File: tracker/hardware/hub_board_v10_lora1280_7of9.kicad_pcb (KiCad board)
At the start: 4 copper layers, 72 x 80 mm, 49 parts, among them U1 U1, U2 U2, U3 U3, U5 U5, U6 U6, U7 U7

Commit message: fix(hub): the operator's routing was 37 copper GRAPHICS, not tracks -- convert and locate the 5 violations
MEASURED, and it explains two separate symptoms the operator reported:

  "the mouse currently doesn't select them successfully"

His interactive pass produced NO track segments. It produced 37 `gr_line` graphics on copper layers,
each carrying a net: /SPI1_SCK 18, /E28_DIO3 7, /E28_BUSY 4, /E28_RESET_N 3, /I2C_SCL 2, /E28_DIO1 2,
/I2C_SDA 1. KiCad treats a net-aware graphic as conductive, so connectivity and DRC both looked
satisfied and no unconnected item named SPI1_SCK or E28_DIO3 -- the nets really are connected.

But a graphic is not a track:
  * selection is governed by the GRAPHICS filter, not TRACKS, which is exactly why clicking one with
    only Tracks enabled selects nothing (and why a finer grid was never going to help);
  * pressing D/M treats it as a drawing, not a routed track, so it does not behave as hand-routing;
  * the interactive router will not shove or re-route it;
  * every tool here that walks board.GetTracks() -- both maze routers, the rip-up pass, the grid and
    validator tests, the connectivity census -- CANNOT SEE THE NET AT ALL. "9/9 routed" was true for
    KiCad and false for our automation, which is the worse kind of green.

FIX: tracker/hardware/tmp_probes/graphics_to_tracks.py recreates each graphic as a PCB_TRACK with the
same layer, width and endpoints (arcs segmented), then deletes the graphic. Applied: 37 graphics ->
37 tracks, and DRC is bit-for-bit unchanged afterwards -- 79 violations, 5 clearance, 0 shorts,
0 mask bridges, same 86 unconnected. So the conversion cost nothing and every net is now visible to
the tooling.

THE FIVE VIOLATIONS, LOCATED PROPERLY
The DRC report's item `pos` is the object's own reference point, NOT the closest approach. The first
figure I drew put its markers ~3 mm off the real gaps; a vision review rejected it while the numbers
were right. tracker/hardware/tmp_probes/plot_clearance_violati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
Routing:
- net /SPI1_SCK: track 0.00 -> 50.7 mm
- net /E28_DIO3: track 0.00 -> 37.9 mm
- net /I2C_SCL: track 27.2 -> 44.9 mm
- net /E28_RESET_N: track 54.4 -> 70.7 mm
- net /E28_DIO1: track 57.4 -> 73.3 mm
- net /E28_BUSY: track 42.7 -> 53.8 mm
- net /I2C_SDA: track 45.4 -> 48.5 mm

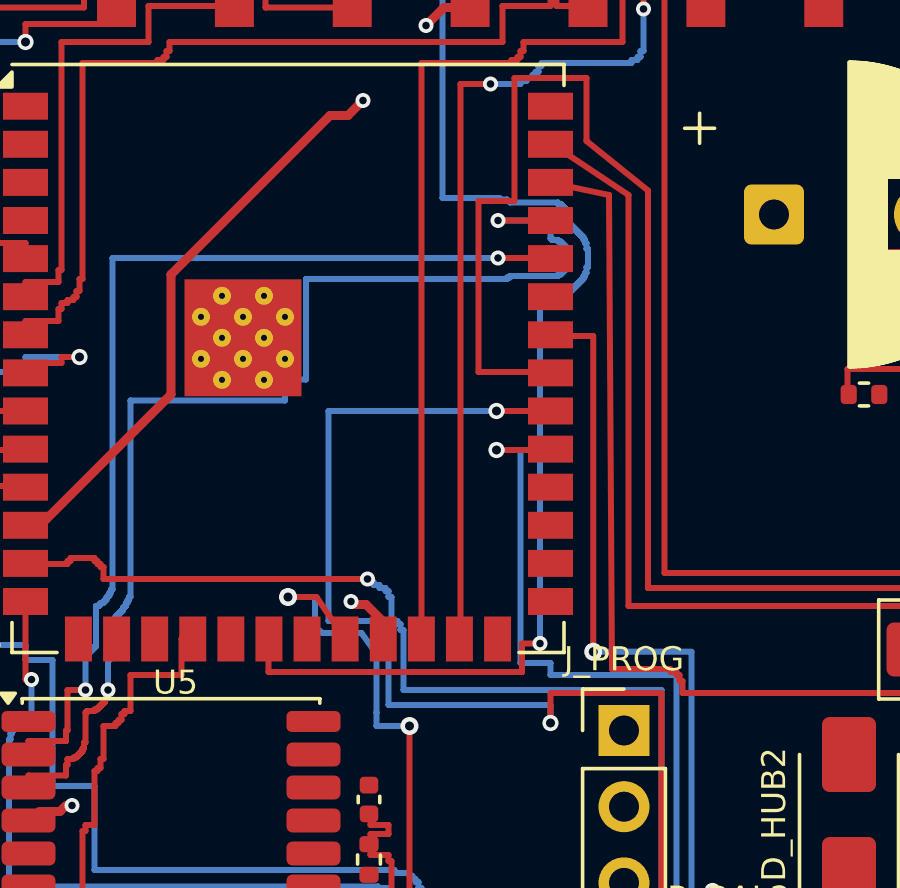
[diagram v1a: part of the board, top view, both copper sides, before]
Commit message: fix(hub): clear the 5 clearance violations on the LoRa1280 interface
Nudged the three corridors: I2C_SDA/I2C_SCL (0.1606 -> >=0.200),
SPI1_SCK/E28_RESET_N on B.Cu (0.1487), and SPI1_SCK vs U1 pad 21
F33_VSENSE (0.1533). Zones refilled before DRC. No rule relaxation.
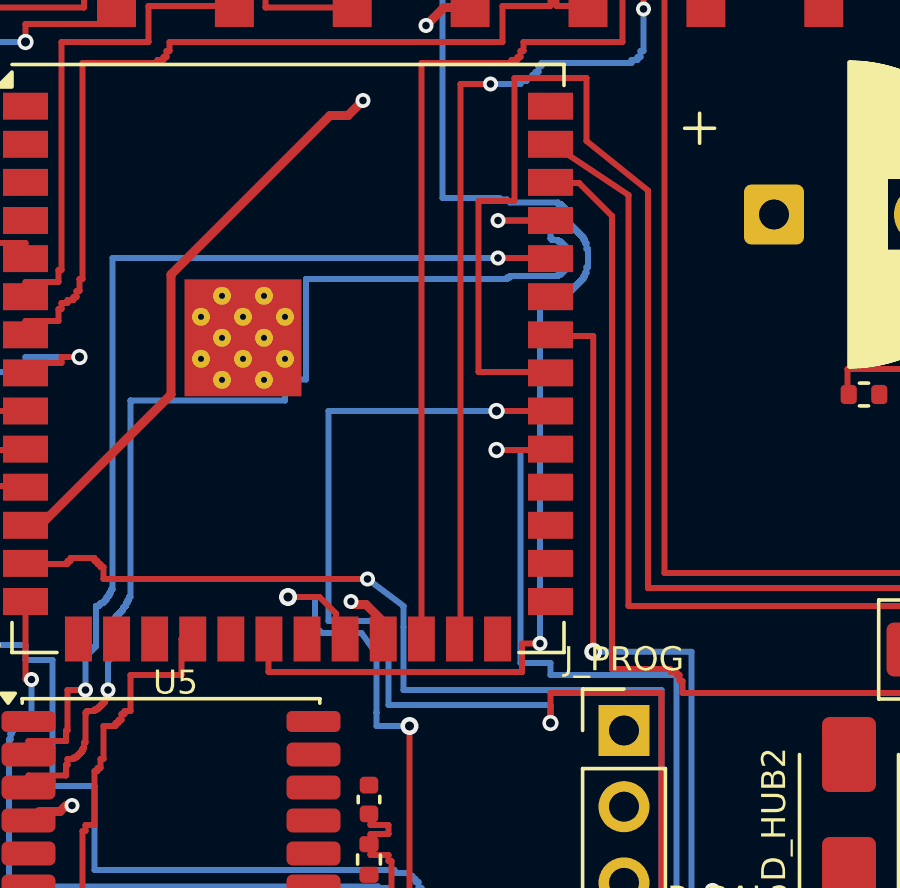
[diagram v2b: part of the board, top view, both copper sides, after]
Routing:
- net /USB_DN: track 36.1 -> 33.4 mm
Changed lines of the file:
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@@
 		)
 	)
+	(gr_line
+		(start 23.65 50.55)
+		(end 22.45 49.65)
+		(stroke
+			(width 0.2)
+			(type default)
+		)
+		(layer "B.Cu")
+		(net 47)
+	)
+	(gr_line
+		(start 23.65 51.25)
+		(end 23.65 50.55)
+		(stroke
+			(width 0.2)
+			(type default)
+		)
+		(layer "B.Cu")
+		(net 47)
+	)
 	(gr_rect
 		(start 0 0)
@@
 	)
 	(segment
-		(start 32.55 52.65)
-		(end 32.55 52.75)
+		(start 54.25 54.95)
+		(end 55.45 54.95)
 		(width 0.2)
 		(layer "F.Cu")
@@
 	)
 	(segment
-		(start 54.25 54.15)
-		(end 54.25 54.95)
+		(start 51.05 53.45)
+		(end 51.05 54.15)
 		(width 0.2)
 		(layer "F.Cu")
@@
 	)
 	(segment
-		(start 51.05 54.15)
-		(end 54.25 54.15)
+		(start 29.5 36.45)
+		(end 30.6 37.55)
 		(width 0.2)
 		(layer "F.Cu")
@@
 	)
 	(segment
-		(start 32.75 52.85)
-		(end 32.85 52.85)
+		(start 32.85 53.05)
+		(end 32.95 53.05)
 		(width 0.2)
 		(layer "F.Cu")
@@
 	)
 	(segment
-		(start 32.75 52.75)
-		(end 32.75 52.85)
+		(start 32.95 53.05)
+		(end 32.95 53.45)
 		(width 0.2)
 		(layer "F.Cu")
@@
 	)
 	(segment
-		(start 32.95 53.05)
-		(end 32.95 53.45)
+		(start 32.55 52.65)
+		(end 32.55 52.75)
 		(width 0.2)
 		(layer "F.Cu")
@@
 	)
 	(segment
-		(start 28.6 36.45)
-		(end 30.5 36.85)
+		(start 30.6 37.55)
+		(end 30.6 52.65)
 		(width 0.2)
 		(layer "F.Cu")
@@
 	)
 	(segment
-		(start 54.25 54.95)
-		(end 55.45 54.95)
+		(start 32.95 53.45)
+		(end 51.05 53.45)
 		(width 0.2)
 		(layer "F.Cu")
@@
 	)
 	(segment
-		(start 32.95 53.45)
-		(end 51.05 53.45)
+		(start 32.75 52.85)
+		(end 32.85 52.85)
 		(width 0.2)
 		(layer "F.Cu")
@@
 	)
 	(segment
-		(start 51.05 53.45)
-		(end 51.05 54.15)
+		(start 32.85 52.85)
+		(end 32.85 53.05)
 		(width 0.2)
 		(layer "F.Cu")
@@
 	)
 	(segment
-		(start 32.85 53.05)
-		(end 32.95 53.05)
+		(start 32.55 52.75)
+		(end 32.75 52.75)
 		(width 0.2)
 		(layer "F.Cu")
@@
 	)
 	(segment
-		(start 30.5 36.85)
-		(end 30.6 52.65)
+		(start 28.6 36.45)
+		(end 29.5 36.45)
 		(width 0.2)
 		(layer "F.Cu")
@@
 	)
 	(segment
-		(start 30.6 52.65)
-		(end 32.55 52.65)
+		(start 54.25 54.15)
+		(end 54.25 54.95)
 		(width 0.2)
 		(layer "F.Cu")
@@
 	)
 	(segment
-		(start 32.85 52.85)
-		(end 32.85 53.05)
+		(start 32.75 52.75)
+		(end 32.75 52.85)
 		(width 0.2)
 		(layer "F.Cu")
@@
 	)
 	(segment
-		(start 32.55 52.75)
-		(end 32.75 52.75)
+		(start 30.6 52.65)
+		(end 32.55 52.65)
+		(width 0.2)
+		(layer "F.Cu")
+		(net 22)
+	)
+	(segment
+		(start 51.05 54.15)
+		(end 54.25 54.15)
 		(width 0.2)
 		(layer "F.Cu")
@@
 	)
 	(segment
-		(start 22.75 51.05)
-		(end 21.15 51.05)
-		(width 0.2)
-		(layer "B.Cu")
-		(net 33)
-	)
-	(segment
 		(start 48.55 64.45)
 		(end 48.55 62.45)
@@
 	)
 	(segment
-		(start 23.15 53.85)
-		(end 23.15 51.85)
-		(width 0.2)
-		(layer "B.Cu")
-		(net 33)
-	)
-	(segment
-		(start 28.55 53.85)
-		(end 23.15 53.85)
+		(start 22.55 51.05)
+		(end 21.15 51.05)
 		(width 0.2)
 		(layer "B.Cu")
@@
 	)
 	(segment
-		(start 23.05 51.85)
-		(end 23.05 51.65)
+		(start 23.15 53.85)
+		(end 23.15 51.65)
 		(width 0.2)
 		(layer "B.Cu")
@@
 	)
 	(segment
-		(start 22.95 51.65)
-		(end 22.95 51.55)
-		(width 0.2)
-		(layer "B.Cu")
-		(net 33)
-	)
-	(segment
 		(start 21.15 44.05)
 		(end 26.75 44.05)
@@
 	)
 	(segment
-		(start 23.05 51.65)
-		(end 22.95 51.65)
+		(start 35.175 62.45)
+		(end 48.55 62.45)
 		(width 0.2)
 		(layer "B.Cu")
@@
 	)
 	(segment
-		(start 22.75 51.55)
-		(end 22.75 51.05)
+		(start 23.15 51.65)
+		(end 22.55 51.05)
 		(width 0.2)
 		(layer "B.Cu")
@@
 	)
 	(segment
-		(start 22.95 51.55)
-		(end 22.75 51.55)
-		(width 0.2)
-		(layer "B.Cu")
-		(net 33)
-	)
-	(segment
-		(start 35.175 62.45)
-		(end 48.55 62.45)
+		(start 28.55 53.85)
+		(end 23.15 53.85)
 		(width 0.2)
 		(layer "B.Cu")
@@
 	)
 	(segment
-		(start 23.15 51.85)
-		(end 23.05 51.85)
+		(start 21.7 51.65)
+		(end 21.4 51.35)
 		(width 0.2)
-		(layer "B.Cu")
-		(net 33)
+		(layer "F.Cu")
+		(net 34)
 	)
 	(segment
-		(start 43.8 73)
-		(end 45.7 73)
+		(start 21.4 51.35)
+		(end 21.4 50.8)
 		(width 0.2)
 		(layer "F.Cu")
@@
 	)
 	(segment
-		(start 20.75 50.25)
-		(end 19.8 50.25)
+		(start 43.8 73)
+		(end 45.7 73)
 		(width 0.2)
 		(layer "F.Cu")
@@
 	)
 	(segment
-		(start 29.15 61.85)
-		(end 29.15 69.15)
+		(start 21.4 50.8)
+		(end 20.85 50.25)
 		(width 0.2)
 		(layer "F.Cu")
@@
 	)
 	(segment
-		(start 21.7 51.65)
-		(end 20.75 50.25)
+		(start 20.85 50.25)
+		(end 19.8 50.25)
+		(width 0.2)
+		(layer "F.Cu")
+		(net 34)
+	)
+	(segment
+		(start 29.15 61.85)
+		(end 29.15 69.15)
 		(width 0.2)
 		(layer "F.Cu")
@@
 	)
 	(segment
-		(start 23.45 51.05)
-		(end 23.45 51.15)
-		(width 0.2)
-		(layer "B.Cu")
-		(net 47)
-	)
-	(segment
-		(start 23.15 50.05)
-		(end 23.15 50.25)
-		(width 0.2)
-		(layer "B.Cu")
-		(net 47)
-	)
-	(segment
-		(start 22.45 49.75)
-		(end 22.65 49.75)
+		(start 30.95 61.05)
+		(end 30.95 62.35)
 		(width 0.2)
 		(layer "B.Cu")
@@
 	)
 	(segment
-		(start 23.65 53.35)
-		(end 32.25 53.35)
+		(start 32.25 61.05)
+		(end 30.95 61.05)
 		(width 0.2)
 		(layer "B.Cu")
@@
 	)
 	(segment
-		(start 22.65 49.85)
-		(end 22.85 49.85)
+		(start 23.65 51.25)
+		(end 23.65 53.35)
 		(width 0.2)
 		(layer "B.Cu")
@@
 	)
 	(segment
-		(start 23.05 49.95)
-		(end 23.05 50.05)
-		(width 0.2)
-		(layer "B.Cu")
-		(net 47)
-	)
-	(segment
-		(start 23.25 51.05)
-		(end 23.45 51.05)
-		(width 0.2)
-		(layer "B.Cu")
-		(net 47)
-	)
-	(segment
-		(start 23.15 50.25)
-		(end 23.25 50.25)
-		(width 0.2)
-		(layer "B.Cu")
-		(net 47)
-	)
-	(segment
-		(start 22.85 49.85)
-		(end 22.85 49.95)
-		(width 0.2)
-		(layer "B.Cu")
-		(net 47)
-	)
-	(segment
-		(start 22.65 49.75)
-		(end 22.65 49.85)
-		(width 0.2)
-		(layer "B.Cu")
-		(net 47)
-	)
-	(segment
 		(start 22.45 49.65)
 		(end 22.45 49.75)
@@
 	)
 	(segment
-		(start 23.65 51.35)
-		(end 23.65 53.35)
-		(width 0.2)
-		(layer "B.Cu")
-		(net 47)
-	)
-	(segment
-		(start 23.55 51.35)
-		(end 23.65 51.35)
-		(width 0.2)
-		(layer "B.Cu")
-		(net 47)
-	)
-	(segment
-		(start 23.25 50.25)
-		(end 23.25 51.05)
-		(width 0.2)
-		(layer "B.Cu")
-		(net 47)
-	)
-	(segment
-		(start 23.05 50.05)
-		(end 23.15 50.05)
-		(width 0.2)
-		(layer "B.Cu")
-		(net 47)
-	)
-	(segment
-		(start 23.45 51.15)
-		(end 23.55 51.15)
-		(width 0.2)
-		(layer "B.Cu")
-		(net 47)
-	)
-	(segment
-		(start 32.25 61.05)
-		(end 30.95 61.05)
-		(width 0.2)
-		(layer "B.Cu")
-		(net 47)
-	)
-	(segment
-		(start 22.85 49.95)
-		(end 23.05 49.95)
-		(width 0.2)
-		(layer "B.Cu")
-		(net 47)
-	)
-	(segment
-		(start 23.55 51.15)
-		(end 23.55 51.35)
-		(width 0.2)
-		(layer "B.Cu")
-		(net 47)
-	)
-	(segment
-		(start 30.95 61.05)
-		(end 30.95 62.35)
+		(start 23.65 53.35)
+		(end 32.25 53.35)
 		(width 0.2)
 		(layer "B.Cu")
